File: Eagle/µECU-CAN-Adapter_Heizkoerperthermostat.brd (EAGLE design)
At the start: 80 x 63.8 mm, 21 parts, among them IC1 MCP2515, IC2 PCA82C251, Q1 16MHz

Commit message: rework board
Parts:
- moved C7 42.0 mm to (15.9, 16.2), turned to 0 degrees
- moved R8 41.7 mm to (15.9, 12.7)
- moved C3 41.0 mm to (15.9, 20.6)
- moved C4 30.6 mm to (34.6, 25.7)
- moved IC1 29.8 mm to (25.7, 24.8), turned to 90 degrees
- moved Q1 26.8 mm to (40.6, 28.3), turned to 90 degrees
- moved CT12 26.8 mm to (39.7, 4.76)
- moved C5 22.2 mm to (34.6, 30.5), turned to 90 degrees
- moved LED12 20.8 mm to (46.7, 6.35), turned to 90 degrees
- moved IC2 20.3 mm to (54.0, 34.6), turned to 270 degrees
- moved C6 18.3 mm to (51.1, 27.3)
- moved R9 17.0 mm to (56.5, 40.6), turned to 270 degrees
- moved U$1 9.23 mm to (25.4, 6.35)
- moved X1 8.26 mm to (69.5, 37.1)
- moved SV2 8.25 mm to (7.94, 26.0)
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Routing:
- net PB5: track 51.1 -> 16.6 mm, vias 1 -> 0
- net PD2: track 29.6 -> 63.5 mm, vias 1 -> 0
- net PB4: track 56.4 -> 27.3 mm, vias 1 -> 0
- net N$10: track 41.3 -> 18.8 mm, vias 1 -> 0
- net N$7: track 8.18 -> 30.6 mm
- net N$6: track 13.0 -> 34.5 mm
- net PB3: track 43.2 -> 24.2 mm, vias 1 -> 0
- net +5V: track 111.9 -> 129.8 mm
- net N$8: track 43.8 -> 27.2 mm
- net PB2: track 46.1 -> 31.2 mm, vias 1 -> 0
- net PC4: track 34.2 -> 20.5 mm, vias 1 -> 0
- net PD6: track 9.97 -> 19.3 mm
- net N$3: track 16.9 -> 10.9 mm
- net N$5: track 8.43 -> 3.90 mm
- net N$4: track 20.3 -> 16.7 mm
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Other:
- board size 80 x 63.8 mm -> 80 x 53 mm

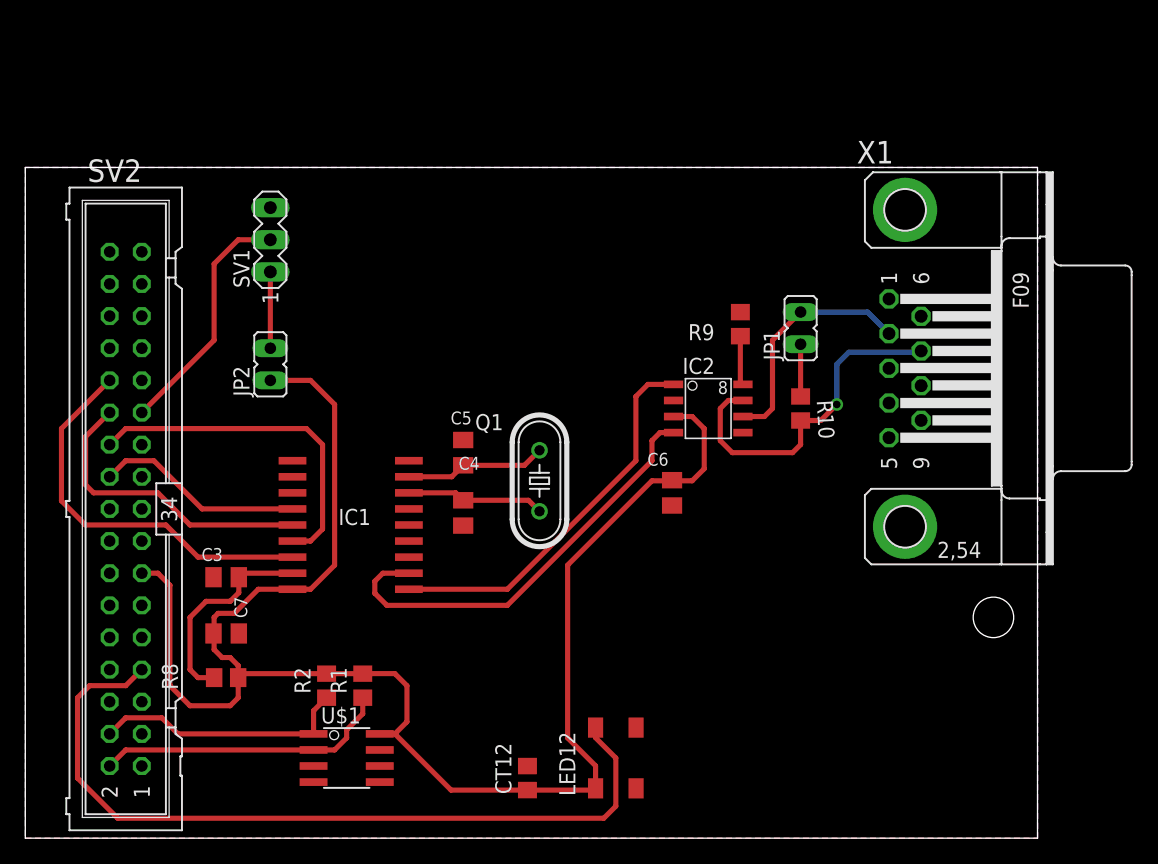
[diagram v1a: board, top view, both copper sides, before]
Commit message: new CAN-Controller
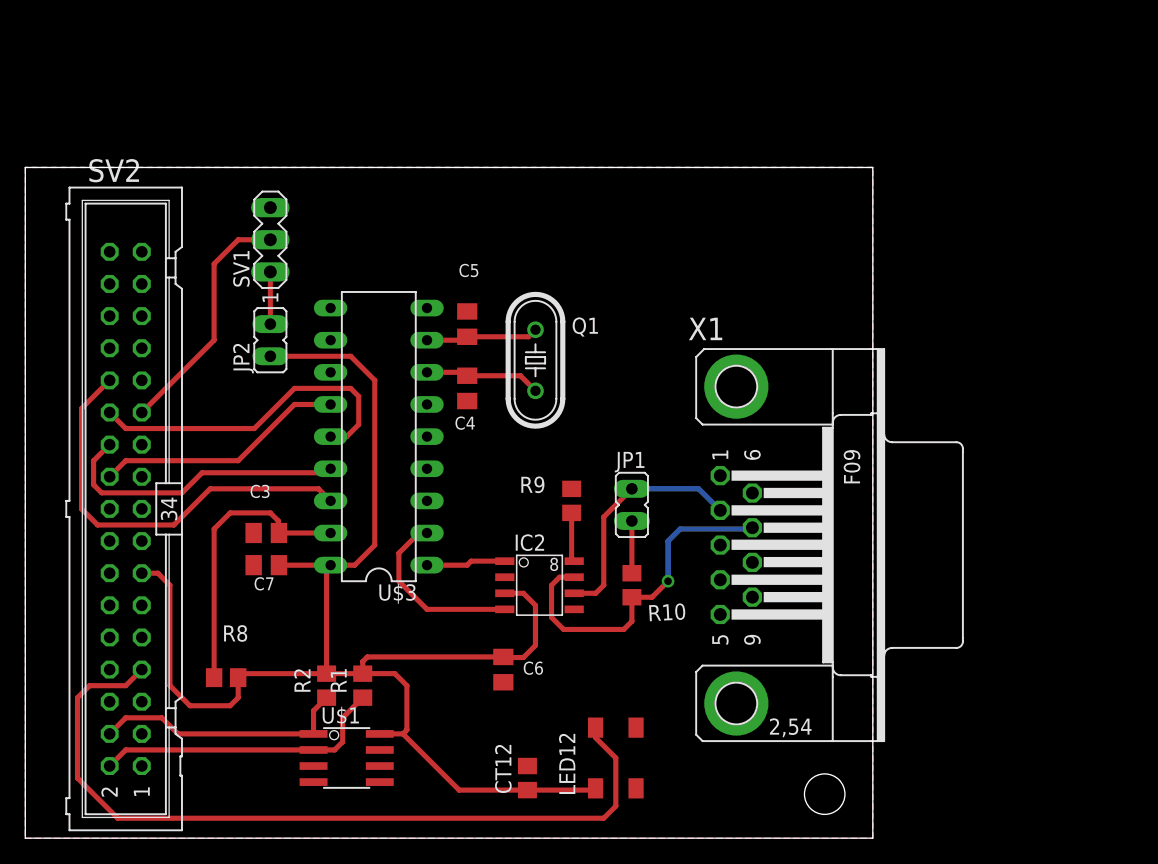
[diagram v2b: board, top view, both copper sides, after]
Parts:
- removed IC1: MCP2515, sp2:SO-18DW
- added U$3: MCP2515PDIP, sp2:DIL18
- moved IC2 19.3 mm to (40.6, 20.6)
- moved X1 19.3 mm to (56.2, 23.2)
- moved C6 19.3 mm to (37.8, 13.3)
- moved JP1 19.3 mm to (47.9, 26.4)
- moved R9 19.3 mm to (43.2, 26.7)
- moved R10 19.3 mm to (47.9, 20.0)
- moved C5 10.2 mm to (34.9, 40.6)
- moved C4 9.85 mm to (34.9, 35.6)
- moved Q1 9.53 mm to (40.3, 37.8)
- moved C7 6.26 mm to (19.1, 21.6), turned to 180 degrees
- moved C3 4.72 mm to (19.1, 24.1)
- moved JP2 1.90 mm to (19.4, 39.4)
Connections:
- net +5V: now also U$3.18; no longer IC1.18
- net GND: now also U$3.9; no longer IC1.9
- net N$2: now also U$3.8; no longer IC1.8
- net N$3: now also U$3.7; no longer IC1.7
- net N$4: now also U$3.17; no longer IC1.17
- net N$6: now also U$3.2; no longer IC1.2
- net N$7: now also U$3.1; no longer IC1.1
- net PB2: now also U$3.16; no longer IC1.16
- net PB3: now also U$3.14; no longer IC1.14
- net PB4: now also U$3.15; no longer IC1.15
- net PB5: now also U$3.13; no longer IC1.13
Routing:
- net N$7: track 30.6 -> 6.28 mm
- net N$6: track 34.5 -> 14.4 mm
- net +5V: track 129.8 -> 115.6 mm
- net N$4: track 16.7 -> 22.7 mm
- net PB4: track 27.3 -> 23.5 mm
- net PB5: track 16.6 -> 19.8 mm
- net PB3: track 24.2 -> 26.6 mm
- net N$2: track 11.2 -> 8.91 mm
- net N$16: track 6.03 -> 4.13 mm
- net N$3: track 10.9 -> 9.18 mm
- net PB2: track 31.2 -> 32.9 mm
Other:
- board size 80 x 53 mm -> 67 x 53 mm
